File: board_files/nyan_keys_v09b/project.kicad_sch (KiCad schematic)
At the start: 140 parts, among them J1 HRO-TYPE-C-31-M-12, J2 Conn_ARM_SWD_TagConnect_TC2030, K1 KEYSW, K10 KEYSW, K11 KEYSW, K12 KEYSW, K13 KEYSW, K14 KEYSW, K15 KEYSW, K16 KEYSW, K17 KEYSW, K18 KEYSW, K19 KEYSW, K2 KEYSW, K20 KEYSW, K21 KEYSW, K22 KEYSW, K23 KEYSW, K24 KEYSW, K25 KEYSW, K26 KEYSW, K27 KEYSW, K28 KEYSW, K29 KEYSW, K3 KEYSW, K30 KEYSW, K31 KEYSW, K32 KEYSW, K33 KEYSW, K34 KEYSW, K35 KEYSW, K36 KEYSW, K37 KEYSW, K38 KEYSW, K39 KEYSW, K4 KEYSW, K40 KEYSW, K41 KEYSW, K42 KEYSW, K43 KEYSW, K44 KEYSW, K45 KEYSW, K46 KEYSW, K47 KEYSW, K48 KEYSW, K49 KEYSW, K5 KEYSW, K50 KEYSW, K51 KEYSW, K52 KEYSW, K53 KEYSW, K54 KEYSW, K55 KEYSW, K56 KEYSW, K57 KEYSW, K58 KEYSW, K59 KEYSW, K6 KEYSW, K60 KEYSW, K61 KEYSW, K7 KEYSW, K8 KEYSW, K9 KEYSW, U1 ICE40HX4K-TQ144, U2 TPS70345, U3 STM32F723VETx, U4 24LC1025, X1 SG-5032CAN, X2 SG-5032CAN

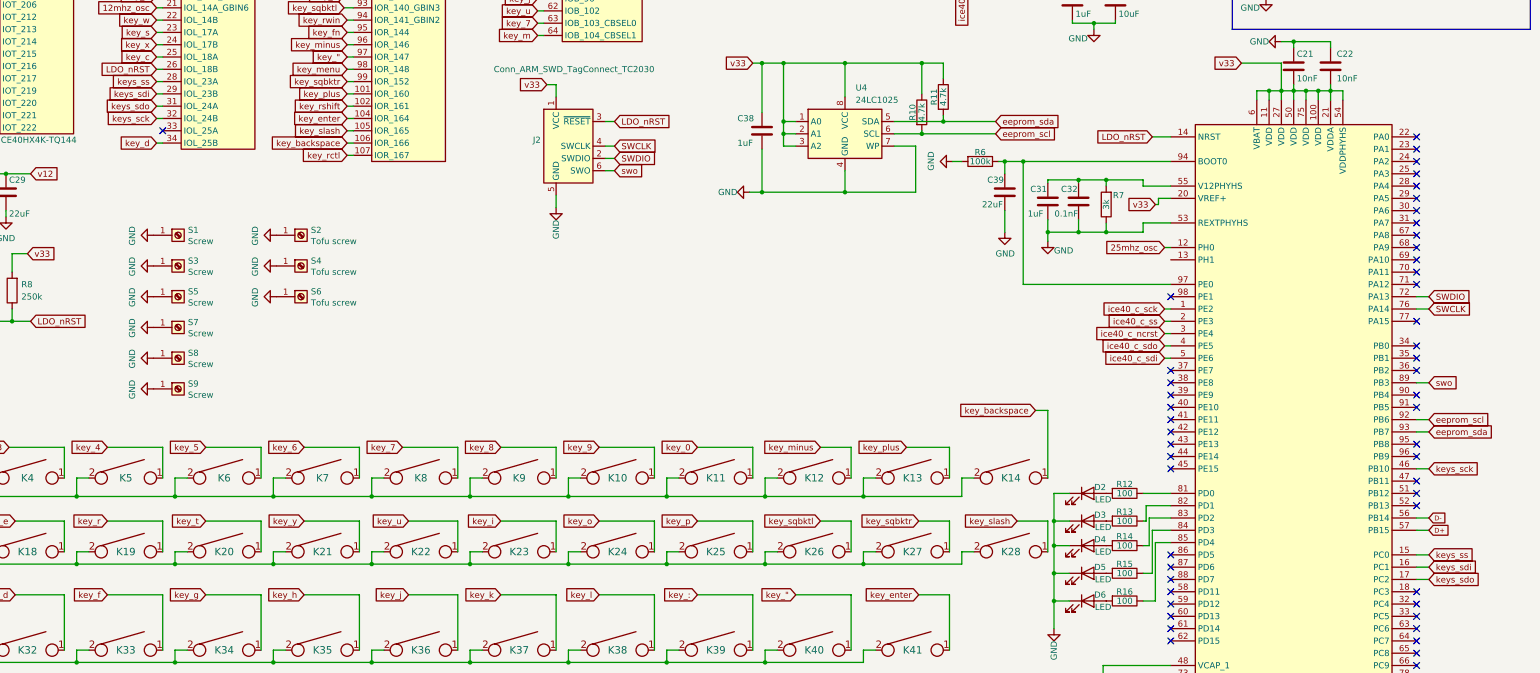
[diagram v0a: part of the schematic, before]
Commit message: R7 patch
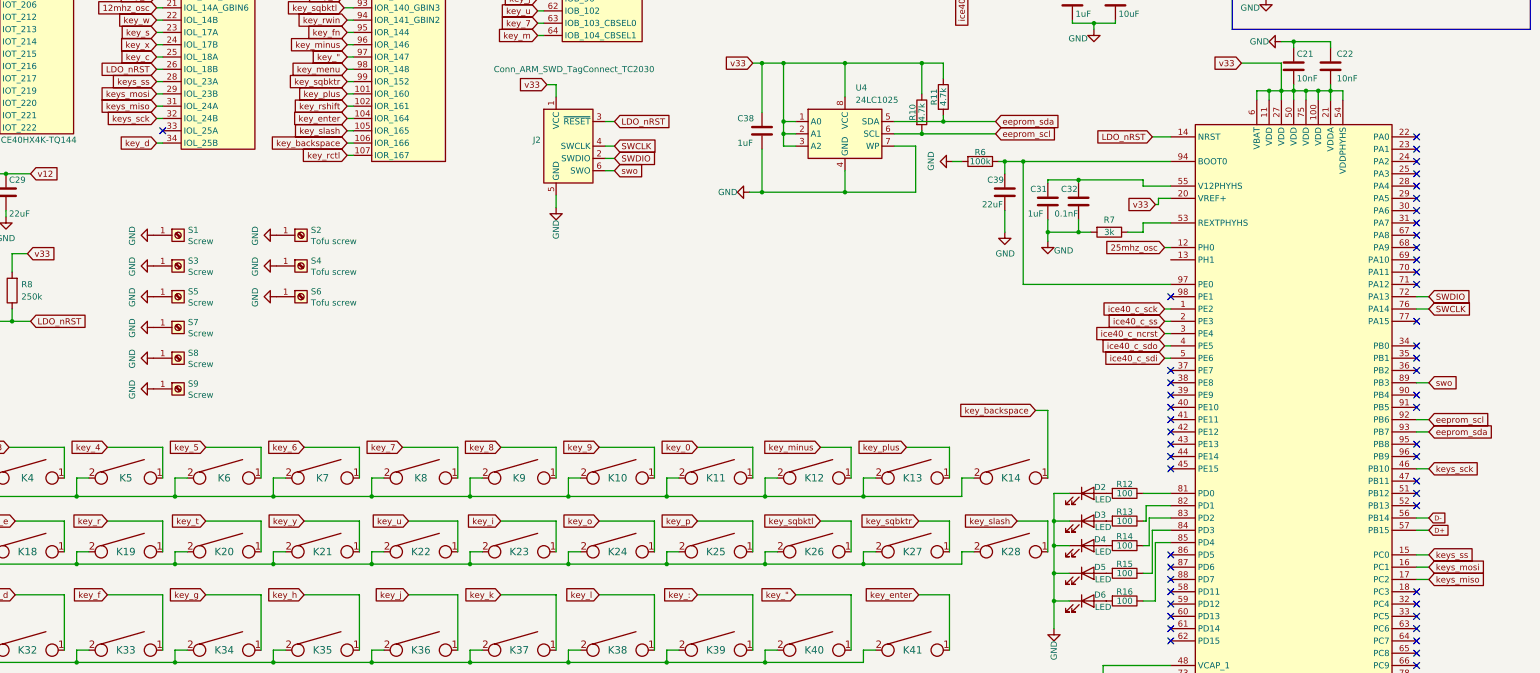
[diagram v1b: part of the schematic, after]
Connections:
- net GND: now also R7.2; no longer R7.1, U3.53 (REXTPHYHS)
- net at C31.2, C32.2, U3.55 (V12PHYHS): no longer R7.2
- net keys_sdi renamed keys_mosi
- net keys_sdo renamed keys_miso
- new net: R7.1, U3.53 (REXTPHYHS)
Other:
- moved on the sheet: R7
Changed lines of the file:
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@@
   (junction (at 377.825 19.05) (diameter 0) (color 0 0 0 0)
   )
-  (junction (at 310.515 121.285) (diameter 0) (color 0 0 0 0)
-  )
   (junction (at 310.515 110.49) (diameter 0) (color 0 0 0 0)
   )
@@
   (junction (at 205.105 230.505) (diameter 0) (color 0 0 0 0)
   )
-  (junction (at 316.23 110.49) (diameter 0) (color 0 0 0 0)
-  )
   (junction (at 249.555 98.425) (diameter 0) (color 0 0 0 0)
   )
@@
   (junction (at 22.225 210.185) (diameter 0) (color 0 0 0 0)
   )
-  (junction (at 316.23 121.285) (diameter 0) (color 0 0 0 0)
-  )
   (junction (at 48.26 40.005) (diameter 0) (color 0 0 0 0)
   )
@@
   (junction (at 83.185 230.505) (diameter 0) (color 0 0 0 0)
   )
+  (junction (at 310.515 121.285) (diameter 0) (color 0 0 0 0)
+  )
   (junction (at 377.19 41.91) (diameter 0) (color 0 0 0 0)
   )
@@
     (stroke (width 0) (type default))
   )
-  (wire (pts (xy 316.23 121.285) (xy 323.85 121.285))
-    (stroke (width 0) (type default))
-  )
   (wire (pts (xy 266.065 187.325) (xy 268.605 187.325))
     (stroke (width 0) (type default))
@@
     (stroke (width 0) (type default))
   )
+  (wire (pts (xy 320.675 121.285) (xy 323.85 121.285))
+    (stroke (width 0) (type default))
+  )
   (wire (pts (xy 144.145 189.865) (xy 164.465 189.865))
     (stroke (width 0) (type default))
@@
     (stroke (width 0) (type default))
   )
-  (wire (pts (xy 310.515 121.285) (xy 316.23 121.285))
-    (stroke (width 0) (type default))
-  )
   (wire (pts (xy 304.165 38.735) (xy 306.07 38.735))
     (stroke (width 0) (type default))
@@
     (stroke (width 0) (type default))
   )
+  (wire (pts (xy 310.515 121.285) (xy 313.055 121.285))
+    (stroke (width 0) (type default))
+  )
   (wire (pts (xy 245.745 189.865) (xy 266.065 189.865))
     (stroke (width 0) (type default))
@@
     (stroke (width 0) (type default))
   )
-  (wire (pts (xy 316.23 110.49) (xy 323.85 110.49))
+  (wire (pts (xy 310.515 110.49) (xy 323.85 110.49))
     (stroke (width 0) (type default))
   )
@@
     (stroke (width 0) (type default))
   )
-  (wire (pts (xy 316.23 119.38) (xy 316.23 121.285))
-    (stroke (width 0) (type default))
-  )
   (wire (pts (xy 158.75 49.53) (xy 160.655 49.53))
     (stroke (width 0) (type default))
@@
     (stroke (width 0) (type default))
   )
-  (wire (pts (xy 316.23 110.49) (xy 310.515 110.49))
-    (stroke (width 0) (type default))
-  )
   (wire (pts (xy 225.425 175.895) (xy 245.745 175.895))
     (stroke (width 0) (type default))
@@
     (stroke (width 0) (type default))
   )
-  (wire (pts (xy 316.23 110.49) (xy 316.23 111.76))
-    (stroke (width 0) (type default))
-  )
   (wire (pts (xy 158.75 72.39) (xy 160.655 72.39))
     (stroke (width 0) (type default))
@@
     )
   )
-  (global_label "keys_sdo" (shape input) (at 382.905 193.04 0) (fields_autoplaced)
+  (global_label "keys_miso" (shape input) (at 382.905 193.04 0) (fields_autoplaced)
     (effects (font (size 1.27 1.27)) (justify left))
-    (property "Intersheetrefs" "${INTERSHEET_REFS}" (at 394.2963 193.04 0)
+    (property "Intersheetrefs" "${INTERSHEET_REFS}" (at 395.4454 193.04 0)
       (effects (font (size 1.27 1.27)) (justify left) hide)
     )
@@
     )
   )
-  (global_label "keys_sdi" (shape input) (at 382.905 190.5 0) (fields_autoplaced)
+  (global_label "keys_mosi" (shape input) (at 382.905 190.5 0) (fields_autoplaced)
     (effects (font (size 1.27 1.27)) (justify left))
-    (property "Intersheetrefs" "${INTERSHEET_REFS}" (at 393.7521 190.5 0)
+    (property "Intersheetrefs" "${INTERSHEET_REFS}" (at 395.4454 190.5 0)
       (effects (font (size 1.27 1.27)) (justify left) hide)
     )
@@
     )
   )
-  (global_label "keys_sdo" (shape input) (at 120.015 95.25 180) (fields_autoplaced)
+  (global_label "keys_miso" (shape input) (at 120.015 95.25 180) (fields_autoplaced)
     (effects (font (size 1.27 1.27)) (justify right))
-    (property "Intersheetrefs" "${INTERSHEET_REFS}" (at 108.6237 95.25 0)
+    (property "Intersheetrefs" "${INTERSHEET_REFS}" (at 107.4746 95.25 0)
       (effects (font (size 1.27 1.27)) (justify right) hide)
     )
@@
     )
   )
-  (global_label "keys_sdi" (shape input) (at 120.015 92.71 180) (fields_autoplaced)
+  (global_label "keys_mosi" (shape input) (at 120.015 92.71 180) (fields_autoplaced)
     (effects (font (size 1.27 1.27)) (justify right))
-    (property "Intersheetrefs" "${INTERSHEET_REFS}" (at 109.1679 92.71 0)
+    (property "Intersheetrefs" "${INTERSHEET_REFS}" (at 107.4746 92.71 0)
       (effects (font (size 1.27 1.27)) (justify right) hide)
     )
@@
     )
   )
-  (symbol (lib_id "Device:R") (at 316.23 115.57 180) (unit 1)
+  (symbol (lib_id "Device:R") (at 316.865 121.285 270) (unit 1)
     (in_bom yes) (on_board yes) (dnp no)
-    (property "Reference" "R7" (at 318.77 113.665 0)
+    (property "Reference" "R7" (at 316.865 118.745 90)
       (effects (font (size 1.27 1.27)))
     )
-    (property "Value" "3k" (at 316.23 115.57 90)
+    (property "Value" "3k" (at 316.865 121.285 90)
       (effects (font (size 1.27 1.27)))
     )
-    (property "Footprint" "Resistor_SMD:R_0402_1005Metric_Pad0.72x0.64mm_HandSolder" (at 318.008 115.57 90)
+    (property "Footprint" "Resistor_SMD:R_0402_1005Metric_Pad0.72x0.64mm_HandSolder" (at 316.865 119.507 90)
       (effects (font (size 1.27 1.27)) hide)
     )
-    (property "Datasheet" "~" (at 316.23 115.57 0)
+    (property "Datasheet" "~" (at 316.865 121.285 0)
       (effects (font (size 1.27 1.27)) hide)
     )
